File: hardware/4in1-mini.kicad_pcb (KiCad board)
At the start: 6 copper layers, 31.2 x 33 mm, 186 parts, among them J1 SM08B-SRSS-TB, Q1 DOY180N03T, Q10 DOY180N03T, Q11 DOY180N03T, Q12 DOY180N03T, Q13 DOY180N03T, Q14 DOY180N03T, Q15 DOY180N03T, Q16 DOY180N03T, Q17 DOY180N03T, Q18 DOY180N03T, Q19 DOY180N03T, Q2 DOY180N03T, Q20 DOY180N03T, Q21 DOY180N03T, Q22 DOY180N03T, Q23 DOY180N03T, Q24 DOY180N03T, Q3 DOY180N03T, Q4 DOY180N03T, Q5 DOY180N03T, Q6 DOY180N03T, Q7 DOY180N03T, Q8 DOY180N03T, Q9 DOY180N03T, U1 TLV76733DRVR, U10 AT32F421G8U7, U11 NSG2065Q, U12 INA186A3IDCKR, U13 LMR54406DBVR, U2 AT32F421G8U7, U3 NSG2065Q, U5 FTC160808S4R7MBCA, U6 AT32F421G8U7, U7 NSG2065Q, U8 AT32F421G8U7, U9 NSG2065Q

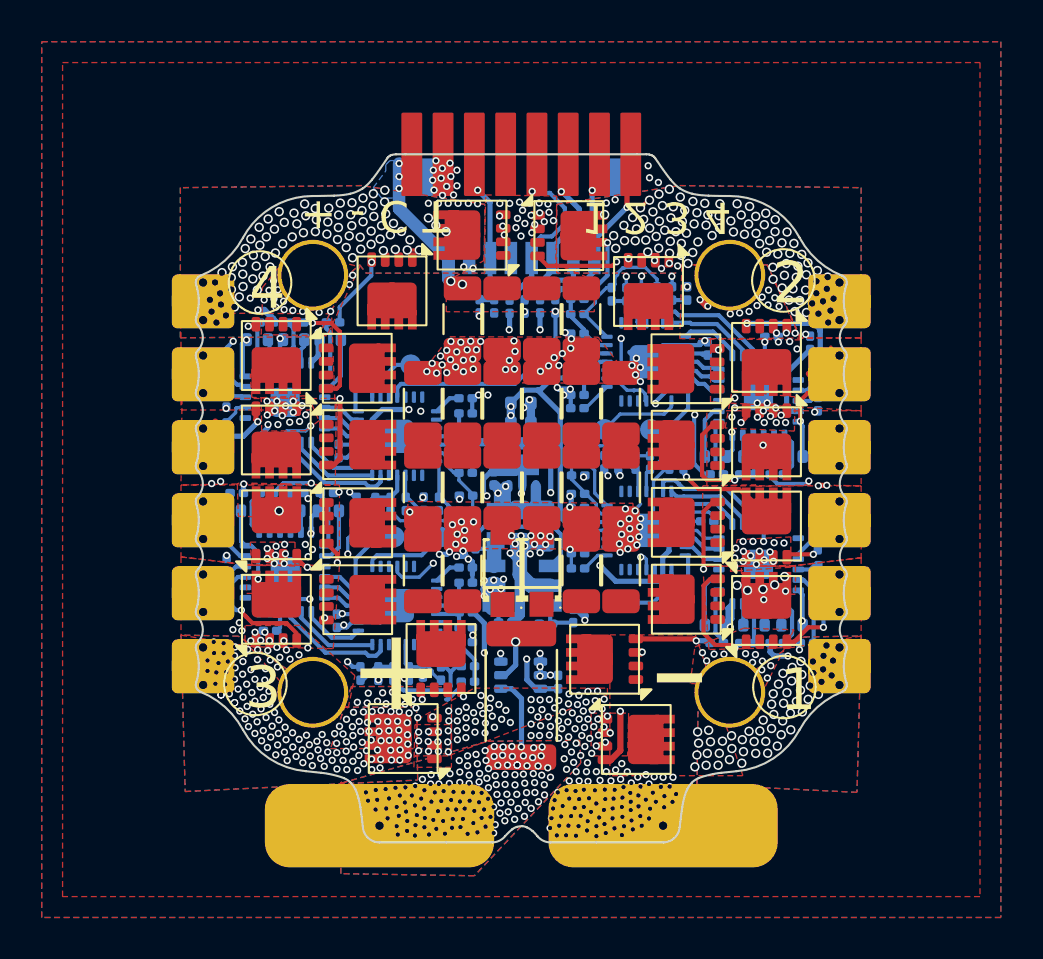
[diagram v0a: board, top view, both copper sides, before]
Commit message: remove MotorA through layer fill on all ESCs to allow for continuous GND pours on inner layers and bottom Cu. Fix Top layer MOSFET arrangement for better placement / routing. DRC pass. Context: https://discord.com/channels/1494019459822653512/1494782966302507118/1530646212594765984
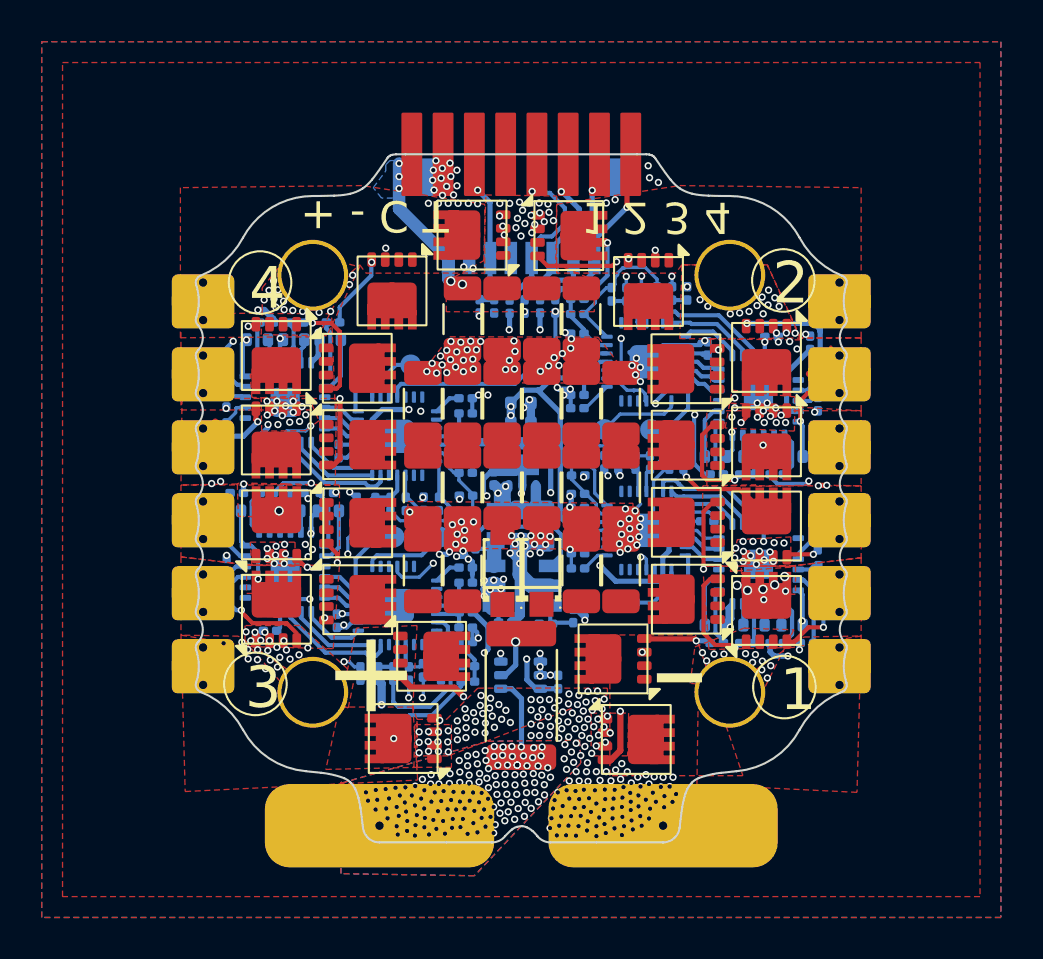
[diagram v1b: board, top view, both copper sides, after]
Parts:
- moved Q13 0.46 mm to (71.7, 56.5), turned to 0 degrees
- moved Q1 0.41 mm to (80.4, 56.6)
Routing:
- net /ESC3/MotorA: track 10.7 -> 14.1 mm, vias 144 -> 3
- net Net-(Q13-G): track 12.6 -> 15.9 mm
- net GND: track 75.7 -> 78.1 mm, vias 457 -> 455
- net /ESC3/MotorB: track 15.9 -> 17.4 mm
- net /ESC3/FBCOMMON: track 6.74 -> 8.01 mm
- net /ESC4/MotorA: track 20.1 -> 19.1 mm, vias 85 -> 3
- net Net-(Q14-G): track 16.4 -> 17.1 mm
- net /ESC2/MotorA: track 14.7 -> 15.2 mm, vias 100 -> 3
- net /ESC1/MotorA: vias 58 -> 3
- removed copper zone on In2.Cu, net +3V3
- removed copper zone on B.Cu, net /ESC1/MotorA
- removed copper zone on In2.Cu, net /ESC1/MotorA
- removed copper zone on In3.Cu, net /ESC1/MotorA
- removed copper zone on B.Cu, net /ESC2/MotorA
- removed copper zone on In2.Cu, net /ESC2/MotorA
- removed copper zone on In3.Cu, net /ESC2/MotorA
- removed copper zone on B.Cu, net /ESC3/MotorA
- removed copper zone on In2.Cu, net /ESC3/MotorA
- removed copper zone on In3.Cu, net /ESC3/MotorA
- removed copper zone on B.Cu, net /ESC4/MotorA
- removed copper zone on In2.Cu, net /ESC4/MotorA
- removed copper zone on In3.Cu, net /ESC4/MotorA
